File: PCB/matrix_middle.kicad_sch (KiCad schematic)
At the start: 68 parts, among them J11 Conn_02x02_Top_Bottom, J12 Conn_02x02_Top_Bottom, J13 Conn_02x02_Top_Bottom, J14 Conn_02x02_Top_Bottom, J15 Conn_02x02_Top_Bottom, J16 Conn_02x02_Top_Bottom, J17 Conn_02x02_Top_Bottom, J18 Conn_02x02_Top_Bottom, J19 Conn_02x02_Top_Bottom, J20 Conn_02x02_Top_Bottom, J21 Conn_02x02_Top_Bottom, J22 Conn_02x02_Top_Bottom

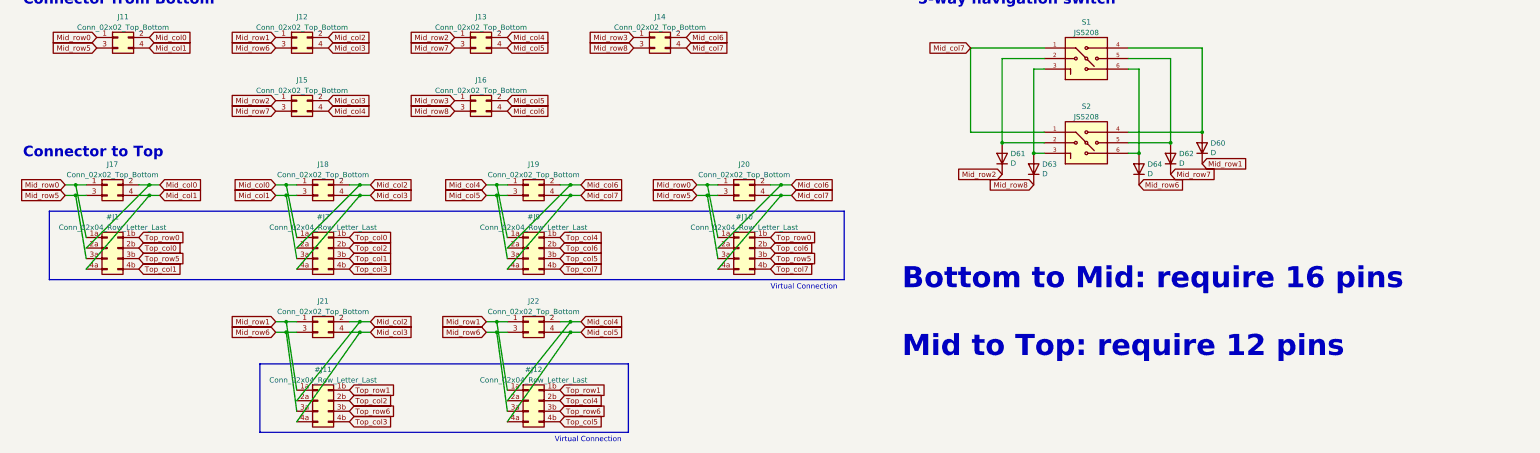
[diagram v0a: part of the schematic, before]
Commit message: JSTコネクタとスペーサーに置き換え
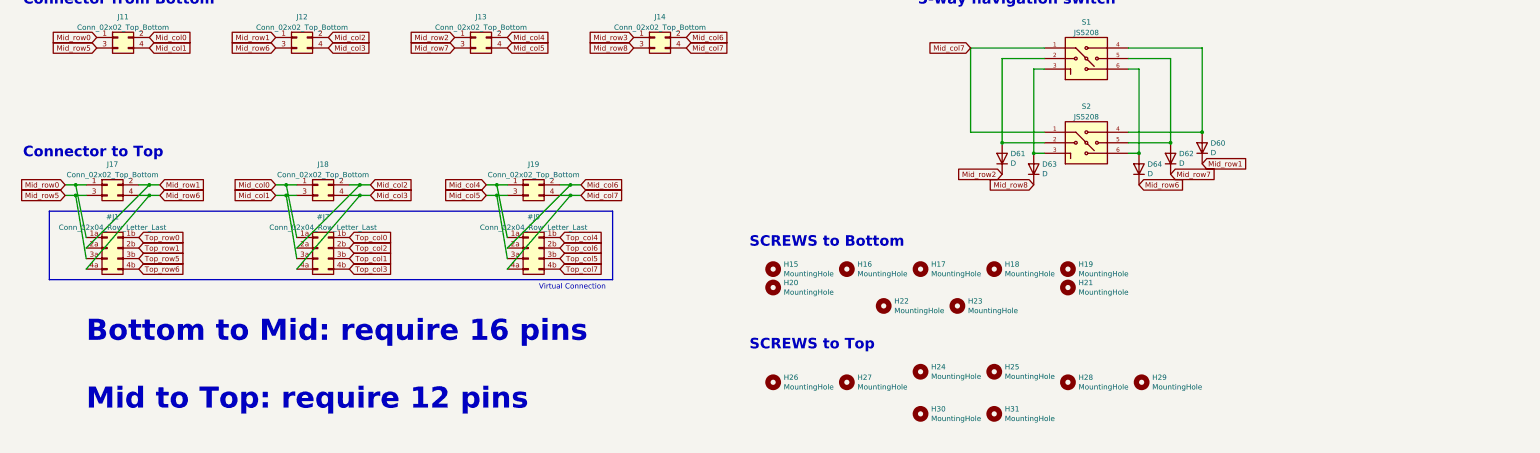
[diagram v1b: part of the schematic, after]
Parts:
- removed #J10, #J11, #J12: Conn_02x04_Row_Letter_Last, symbol Connector_Generic:Conn_02x04_Row_Letter_Last
- removed J15, J16, J20, J21, J22: Conn_02x02_Top_Bottom, locallib:PinHeader_2x02_P2.00mm_Vertical_Centered, symbol Connector_Generic:Conn_02x02_Odd_Even
- added H15, H16, H17, H18, H19, H20, H21, H22, H23, H24, H25, H26, H27, H28, H29, H30, H31: MountingHole, MountingHole:MountingHole_2.2mm_M2_No_Cu, symbol Mechanical:MountingHole
- J11, J12, J13, J14, J17, J18, J19: footprint locallib:PinHeader_2x02_P2.00mm_Vertical_Centered -> Connector_JST:JST_SH_SM04B-SRSS-TB_1x04-1MP_P1.00mm_Horizontal
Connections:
- net Mid_col0: no longer #J1.2a (Pin_2a), J17.2 (Pin_2)
- net Mid_col1: no longer #J1.4a (Pin_4a), J17.4 (Pin_4)
- net Mid_row1: now also #J1.2a (Pin_2a), J17.2 (Pin_2)
- net Mid_row6: now also #J1.4a (Pin_4a), J17.4 (Pin_4)
- net Top_col0: no longer #J1.2b (Pin_2b)
- net Top_col1: no longer #J1.4b (Pin_4b)
- net Top_row1: now also #J1.2b (Pin_2b)
- net Top_row6: now also #J1.4b (Pin_4b)
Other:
- note added: "SCREWS to Bottom"
- note added: "SCREWS to Top"

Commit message: コネクタ位置考え中
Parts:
- added J20, J21, J22, J26, J27, J28, J29: Conn_01x04, Connector_PinHeader_2.54mm:PinHeader_1x04_P2.54mm_Vertical, symbol Connector_Generic:Conn_01x04
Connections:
- net Mid_col0: now also J20.2 (Pin_2), J28.1 (Pin_1)
- net Mid_col1: now also J20.4 (Pin_4), J28.3 (Pin_3)
- net Mid_col2: now also J21.2 (Pin_2), J28.2 (Pin_2)
- net Mid_col3: now also J21.4 (Pin_4), J28.4 (Pin_4)
- net Mid_col4: now also J22.2 (Pin_2), J29.1 (Pin_1)
- net Mid_col5: now also J22.4 (Pin_4), J29.3 (Pin_3)
- net Mid_col6: now also J26.2 (Pin_2), J29.2 (Pin_2)
- net Mid_col7: now also J26.4 (Pin_4), J29.4 (Pin_4)
- net Mid_row0: now also J20.1 (Pin_1), J27.1 (Pin_1)
- net Mid_row1: now also J21.1 (Pin_1), J27.2 (Pin_2)
- net Mid_row2: now also J22.1 (Pin_1)
- net Mid_row3: now also J26.1 (Pin_1)
- net Mid_row5: now also J20.3 (Pin_3), J27.3 (Pin_3)
- net Mid_row6: now also J21.3 (Pin_3), J27.4 (Pin_4)
- net Mid_row7: now also J22.3 (Pin_3)
- net Mid_row8: now also J26.3 (Pin_3)

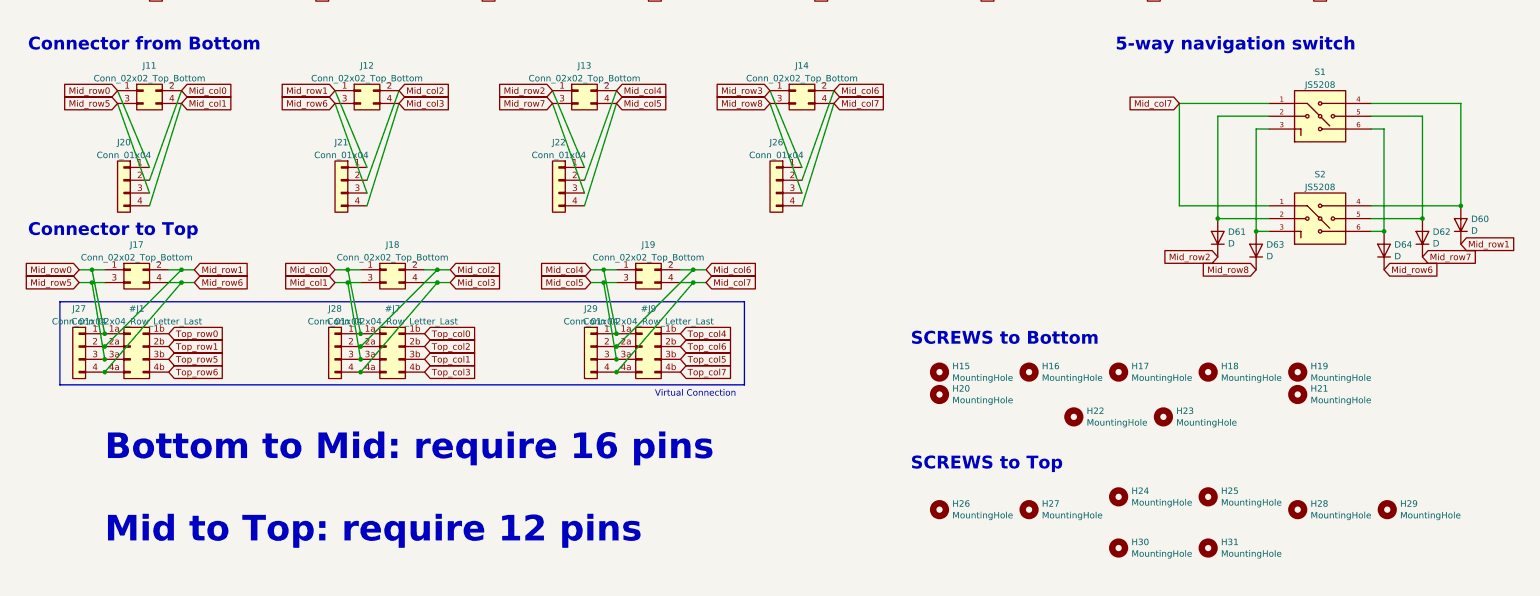
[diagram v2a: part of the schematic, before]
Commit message: 3枚の基板を1枚にまとめ中
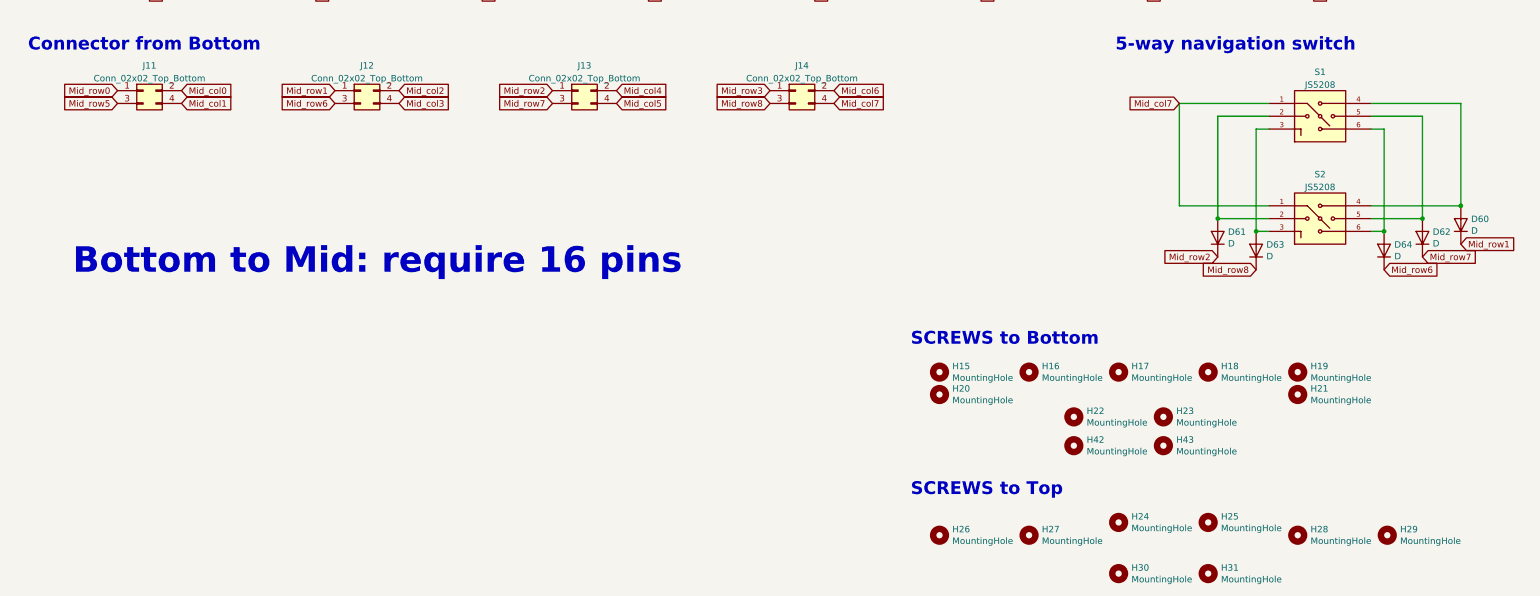
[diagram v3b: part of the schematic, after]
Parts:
- removed #J1, #J7, #J9: Conn_02x04_Row_Letter_Last, symbol Connector_Generic:Conn_02x04_Row_Letter_Last
- removed J17, J18, J19: Conn_02x02_Top_Bottom, Connector_JST:JST_SH_SM04B-SRSS-TB_1x04-1MP_P1.00mm_Horizontal, symbol Connector_Generic:Conn_02x02_Odd_Even
- removed J20, J21, J22, J26, J27, J28, J29: Conn_01x04, Connector_PinHeader_2.54mm:PinHeader_1x04_P2.54mm_Vertical, symbol Connector_Generic:Conn_01x04
- added H42, H43: MountingHole, MountingHole:MountingHole_2.2mm_M2_No_Cu, symbol Mechanical:MountingHole
- J11, J12, J13, J14: footprint Connector_JST:JST_SH_SM04B-SRSS-TB_1x04-1MP_P1.00mm_Horizontal -> locallib:JST_SH_SM04B-SRSS-TB_1x04-1MP_P1.00mm_Horizontal_wCable_housing_spare_pin
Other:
- note added: "Bottom to Mid: require 16 pins"
- note removed: "Bottom to Mid: require 16 pins Mid to Top: require 12 pins"
- note removed: "Connector to Top"
- note removed: "Virtual Connection"
- moved on the sheet: H24, H25, H26, H27, H28, H29, H30, H31

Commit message: 基板外形置き換え
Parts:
- H15, H16, H17, H18, H19, H20, H21, H22, H23, H24, H25, H26, H27, H28, H29, H30, H31, H42, H43: footprint MountingHole:MountingHole_2.2mm_M2_No_Cu -> MountingHole:MountingHole_2.2mm_M2_Pad; symbol Mechanical:MountingHole -> Mechanical:MountingHole_Pad
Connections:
- new net Mid_GND: H15.1, H16.1, H17.1, H18.1, H19.1, H20.1, H21.1, H22.1, H23.1, H24.1, H25.1, H26.1, H27.1, H28.1, H29.1, H30.1, H31.1, H42.1, H43.1

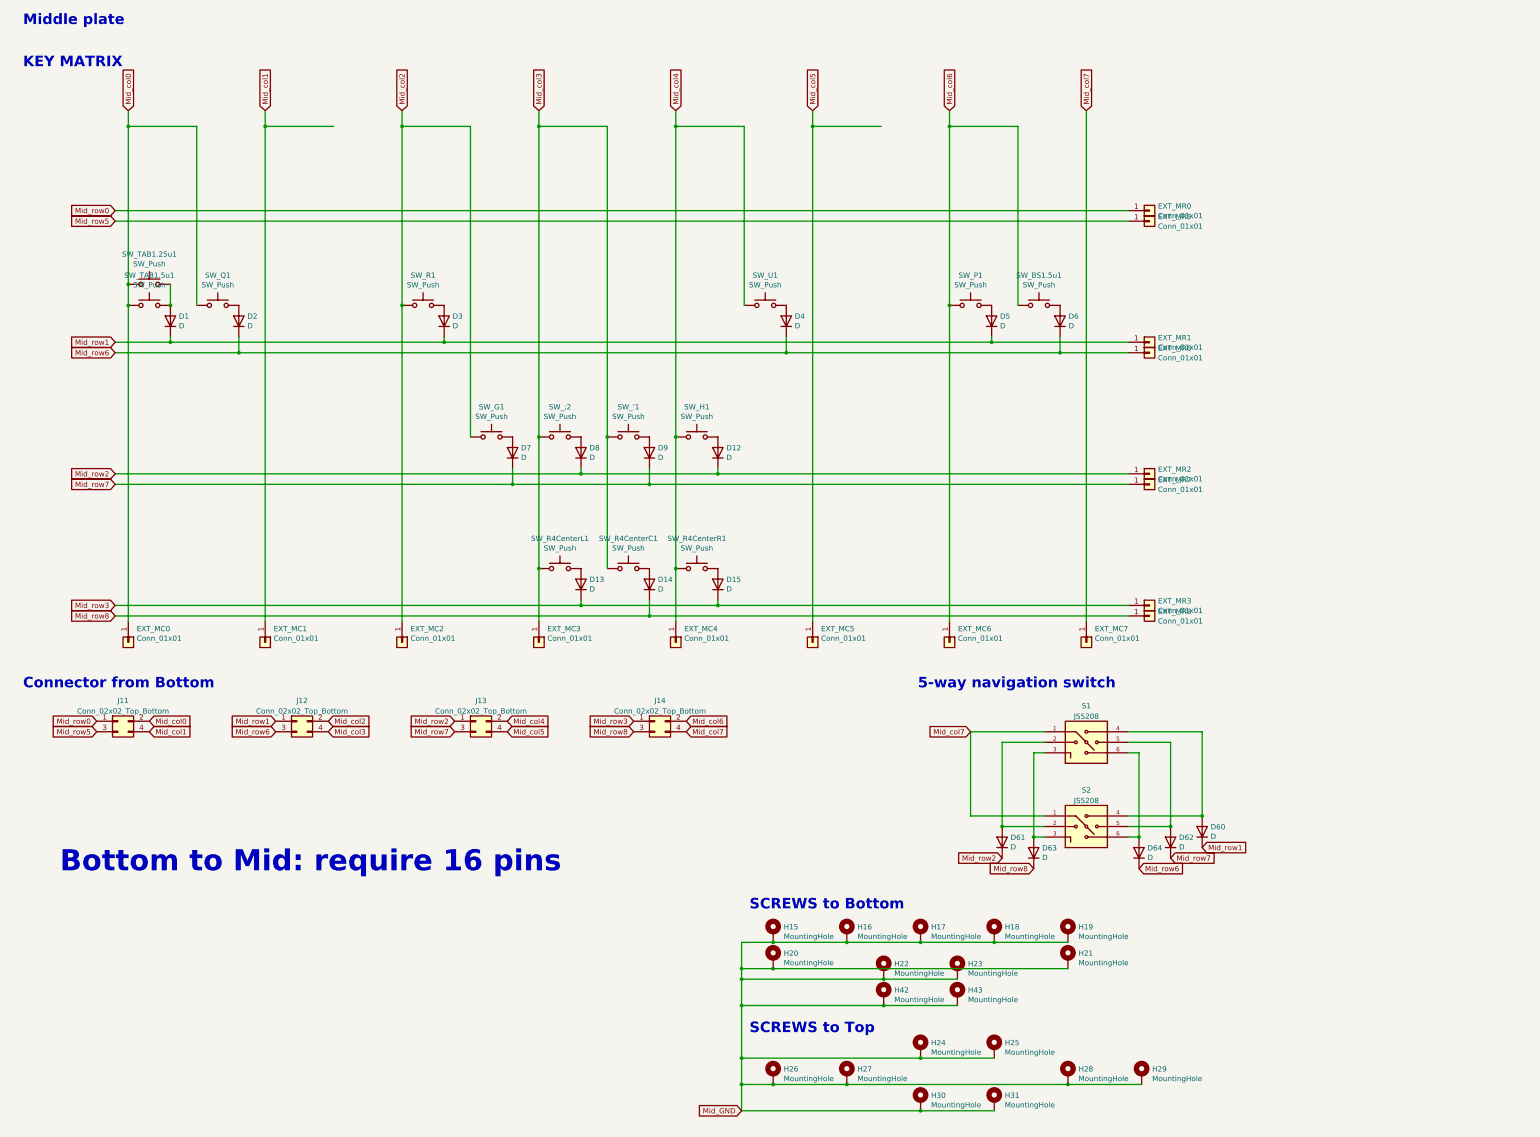
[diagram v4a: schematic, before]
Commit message: BaseからMidへのピン数減少のため、コネクタ1個減らす
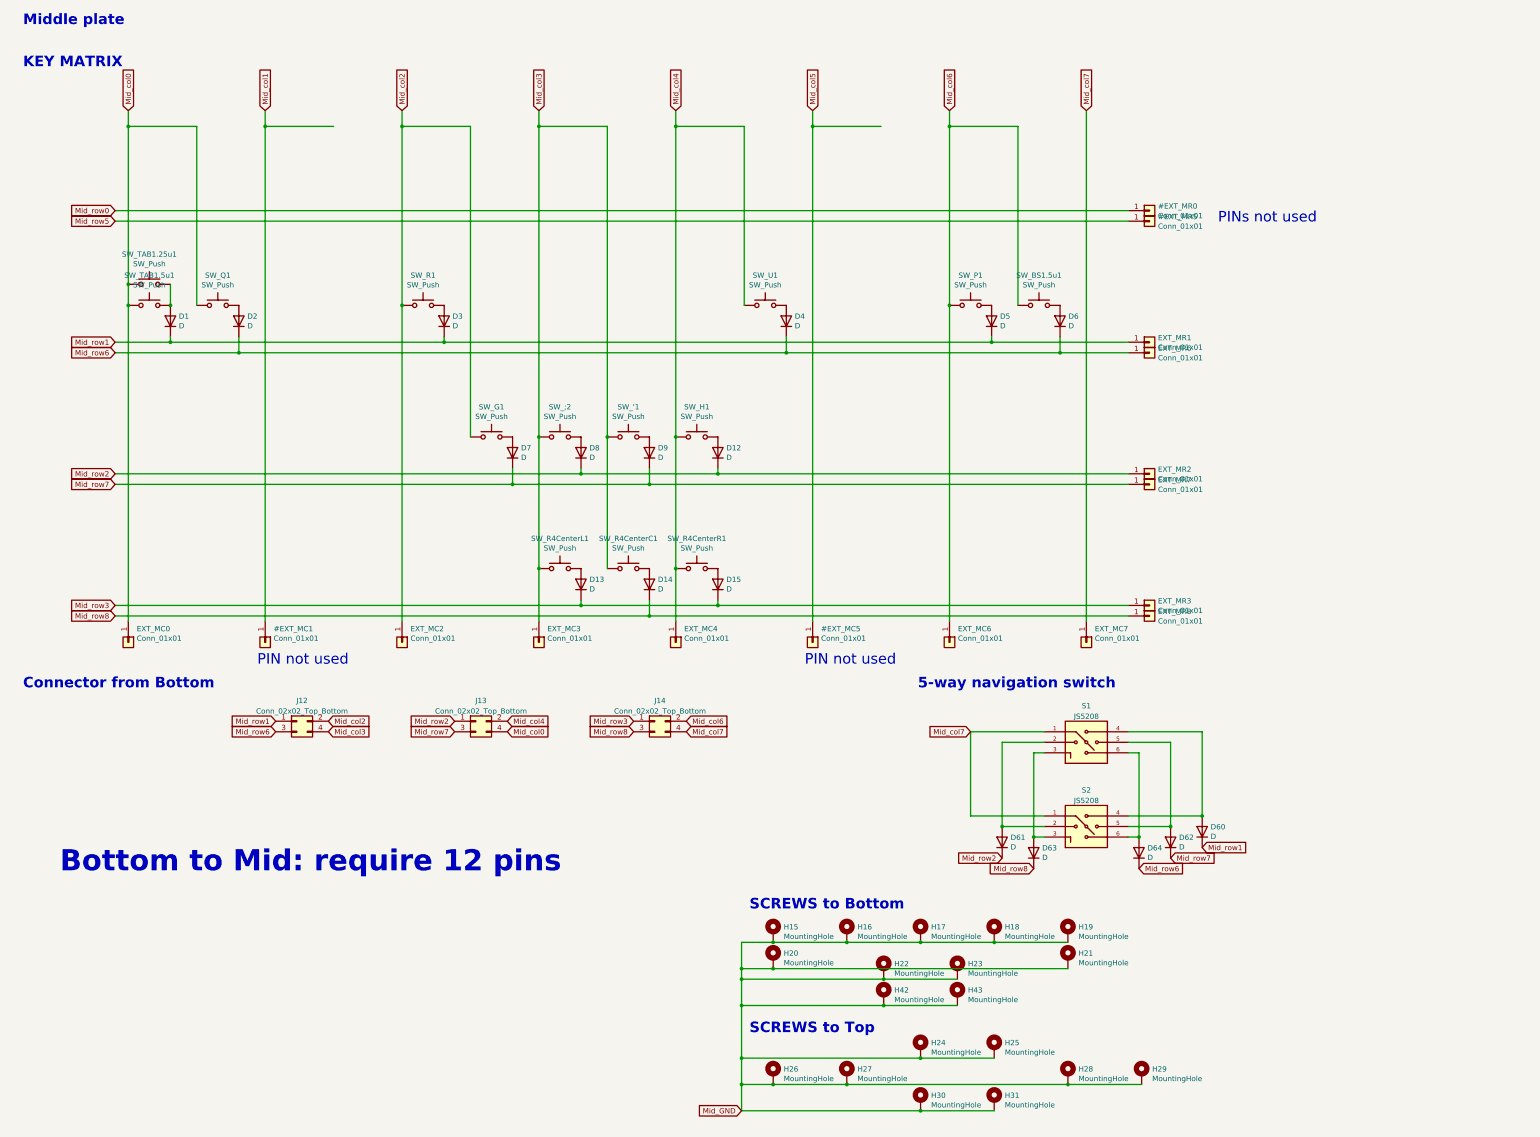
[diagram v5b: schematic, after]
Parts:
- removed EXT_MC1, EXT_MC5, EXT_MR0, EXT_MR5: Conn_01x01, TestPoint:TestPoint_THTPad_D2.0mm_Drill1.0mm, symbol Connector_Generic:Conn_01x01
- removed J11: Conn_02x02_Top_Bottom, locallib:JST_SH_SM04B-SRSS-TB_1x04-1MP_P1.00mm_Horizontal_wCable_housing_spare_pin, symbol Connector_Generic:Conn_02x02_Odd_Even
- H15, H16, H17, H18, H19, H20, H21, H22, H23, H24, H25, H26, H27, H28, H29, H30, H31, H42, H43: footprint MountingHole:MountingHole_2.2mm_M2_Pad -> MountingHole:MountingHole_2.2mm_M2_Pad_minimal
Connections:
- net Mid_col0: now also J13.4 (Pin_4)
- net Mid_col5: no longer J13.4 (Pin_4)
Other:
- note added: "Bottom to Mid: require 12 pins"
- note added: "PIN not used"
- note added: "PINs not used"
- note removed: "Bottom to Mid: require 16 pins"

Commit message: キープレートのフットプリント作成苦戦中
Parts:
- added SW_R2, SW_U2: SW_Push, MX_Alps_Hybrid:MXOnly-1U-NoLED, symbol Switch:SW_Push
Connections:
- net Mid_col2: now also SW_R2.1
- net Mid_col4: now also SW_U2.1
- net at D4.2 (A), SW_U1.2: now also SW_U2.2
- net at D3.2 (A), SW_R1.2: now also SW_R2.2
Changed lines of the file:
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@@
   (junction (at 246.38 93.98) (diameter 0) (color 0 0 0 0)
   )
+  (junction (at 196.85 85.09) (diameter 0) (color 0 0 0 0)
+  )
   (junction (at 211.455 273.05) (diameter 0) (color 0 0 0 0)
   )
+  (junction (at 186.69 80.01) (diameter 0) (color 0 0 0 0)
+  )
   (junction (at 180.34 125.73) (diameter 0) (color 0 0 0 0)
   )
@@
   (junction (at 163.83 160.02) (diameter 0) (color 0 0 0 0)
   )
+  (junction (at 104.14 80.01) (diameter 0) (color 0 0 0 0)
+  )
   (junction (at 236.22 41.91) (diameter 0) (color 0 0 0 0)
   )
@@
   (junction (at 262.89 96.52) (diameter 0) (color 0 0 0 0)
   )
+  (junction (at 114.3 85.09) (diameter 0) (color 0 0 0 0)
+  )
   (wire (pts (xy 281.94 213.36) (xy 281.94 193.04))
     (stroke (width 0) (type default) (color 0 0 0 0))
@@
     (stroke (width 0) (type default) (color 0 0 0 0))
   )
+  (wire (pts (xy 104.14 80.01) (xy 104.14 85.09))
+    (stroke (width 0) (type default) (color 0 0 0 0))
+  )
   (wire (pts (xy 279.4 96.52) (xy 262.89 96.52))
     (stroke (width 0) (type default) (color 0 0 0 0))
@@
     (stroke (width 0) (type default) (color 0 0 0 0))
   )
-  (wire (pts (xy 104.14 41.91) (xy 104.14 85.09))
+  (wire (pts (xy 104.14 41.91) (xy 104.14 80.01))
     (stroke (width 0) (type default) (color 0 0 0 0))
   )
@@
     (stroke (width 0) (type default) (color 0 0 0 0))
   )
-  (wire (pts (xy 186.69 41.91) (xy 186.69 85.09))
+  (wire (pts (xy 186.69 41.91) (xy 186.69 80.01))
     (stroke (width 0) (type default) (color 0 0 0 0))
   )
@@
     (stroke (width 0) (type default) (color 0 0 0 0))
   )
+  (wire (pts (xy 196.85 80.01) (xy 196.85 85.09))
+    (stroke (width 0) (type default) (color 0 0 0 0))
+  )
   (wire (pts (xy 64.77 96.52) (xy 196.85 96.52))
     (stroke (width 0) (type default) (color 0 0 0 0))
@@
     (stroke (width 0) (type default) (color 0 0 0 0))
   )
+  (wire (pts (xy 186.69 80.01) (xy 186.69 85.09))
+    (stroke (width 0) (type default) (color 0 0 0 0))
+  )
   (wire (pts (xy 48.26 92.71) (xy 48.26 93.98))
     (stroke (width 0) (type default) (color 0 0 0 0))
@@
   )
   (wire (pts (xy 211.455 238.76) (xy 229.235 238.76))
+    (stroke (width 0) (type default) (color 0 0 0 0))
+  )
+  (wire (pts (xy 114.3 80.01) (xy 114.3 85.09))
     (stroke (width 0) (type default) (color 0 0 0 0))
   )
@@
     )
     (pin "1")
+  )
+  (symbol (lib_id "Switch:SW_Push") (at 109.22 80.01 0) (unit 1)
+    (in_bom yes) (on_board yes)
+    (property "Reference" "SW_R2" (id 0) (at 109.22 72.771 0))
+    (property "Value" "SW_Push" (id 1) (at 109.22 75.0824 0))
+    (property "Footprint" "MX_Alps_Hybrid:MXOnly-1U-NoLED" (id 2) (at 109.22 74.93 0)
+      (effects (font (size 1.27 1.27)) hide)
+    )
+    (property "Datasheet" "~" (id 3) (at 109.22 74.93 0)
+      (effects (font (size 1.27 1.27)) hide)
+    )
+    (pin "1")
+    (pin "2")
   )
   (symbol (lib_id "Connector_Generic:Conn_01x01") (at 284.48 128.27 0) (unit 1)
@@
     (pin "4")
   )
+  (symbol (lib_id "Switch:SW_Push") (at 191.77 80.01 0) (unit 1)
+    (in_bom yes) (on_board yes)
+    (property "Reference" "SW_U2" (id 0) (at 191.77 72.771 0))
+    (property "Value" "SW_Push" (id 1) (at 191.77 75.0824 0))
+    (property "Footprint" "MX_Alps_Hybrid:MXOnly-1U-NoLED" (id 2) (at 191.77 74.93 0)
+      (effects (font (size 1.27 1.27)) hide)
+    )
+    (property "Datasheet" "~" (id 3) (at 191.77 74.93 0)
+      (effects (font (size 1.27 1.27)) hide)
+    )
+    (pin "1")
+    (pin "2")
+  )
   (symbol (lib_id "Connector_Generic:Conn_01x01") (at 284.48 160.02 0) (unit 1)
